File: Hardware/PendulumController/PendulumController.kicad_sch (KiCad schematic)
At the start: 12 parts, among them J101 MOTOR, J102 ENCODER

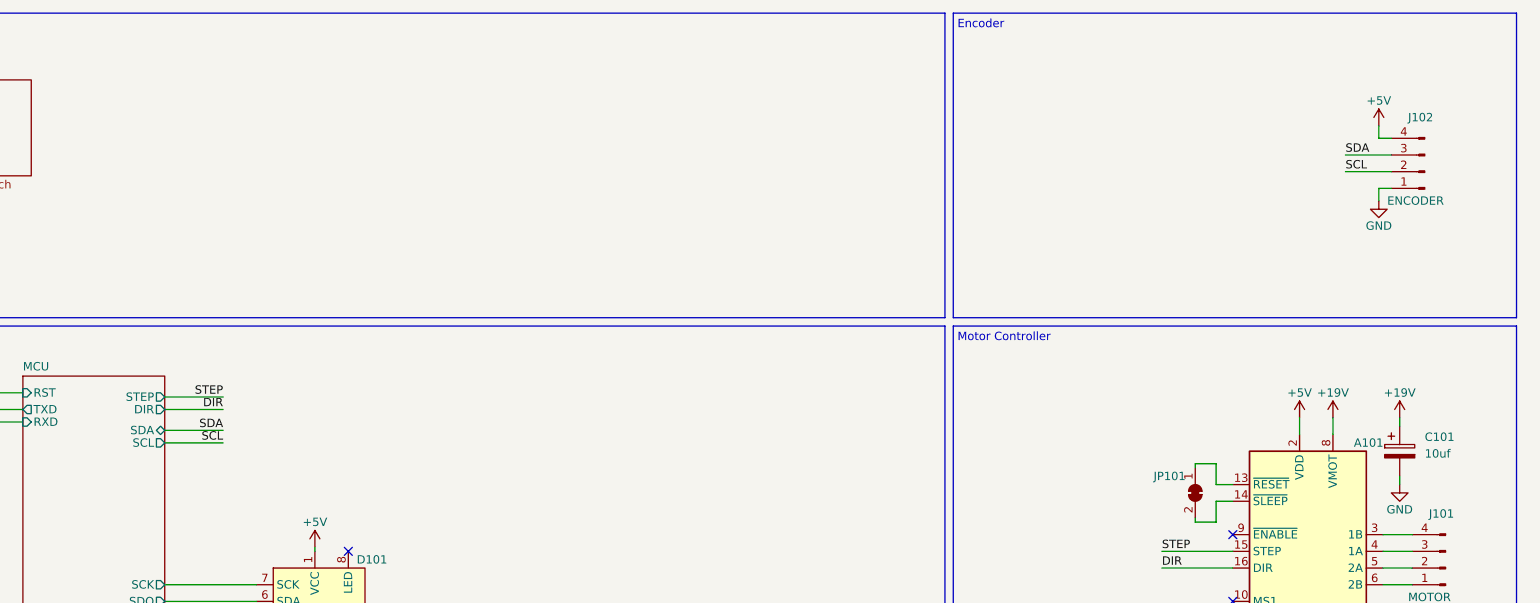
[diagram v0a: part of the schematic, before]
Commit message: Clean up board design with embedded power supply
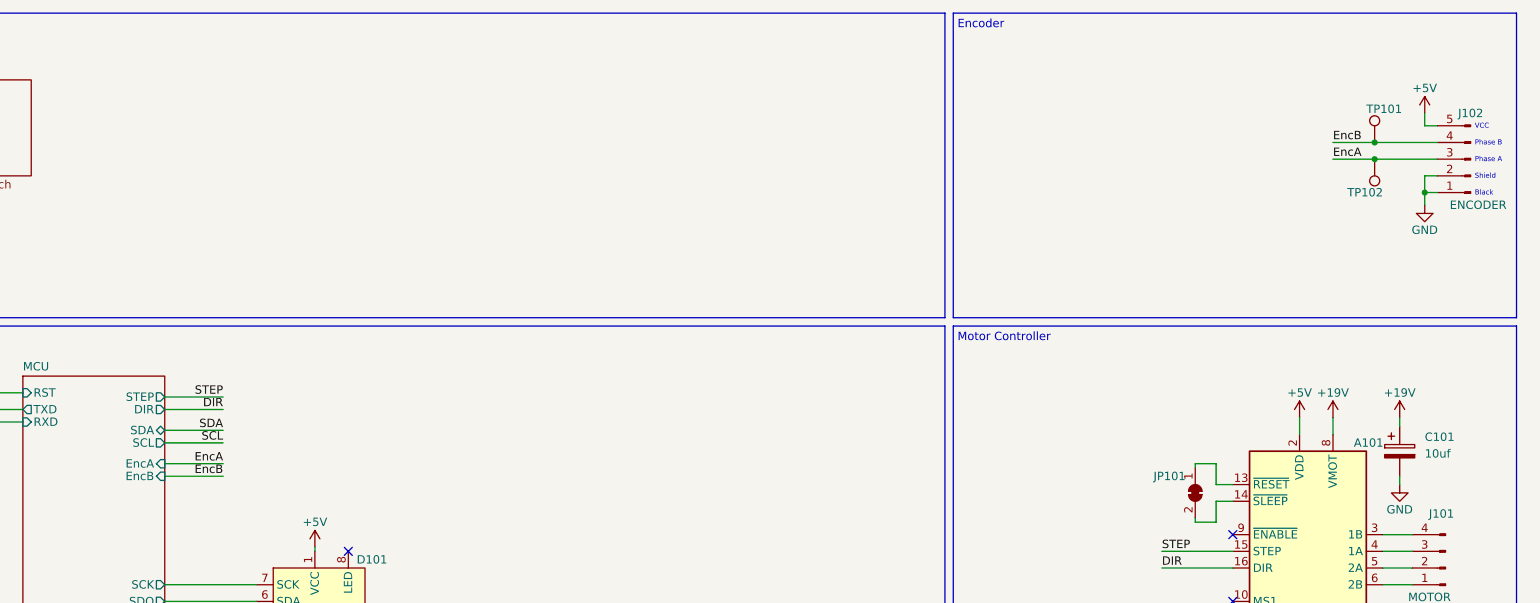
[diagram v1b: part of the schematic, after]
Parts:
- removed J102: ENCODER, Connector_JST:JST_EH_B4B-EH-A_1x04_P2.50mm_Vertical, symbol Connector:Conn_01x04_Male
- added J102: ENCODER, Connector_JST:JST_EH_B5B-EH-A_1x05_P2.50mm_Vertical, symbol Connector:Conn_01x05_Male
- added TP101, TP102: TestPoint, TestPoint:TestPoint_Pad_1.5x1.5mm, symbol Connector:TestPoint
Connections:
- net +5V: now also J102.5 (Pin_5)
- net GND: now also J102.1 (Pin_1), J102.2 (Pin_2)
- new net EncA: J102.3 (Pin_3), TP102.1
- new net EncB: J102.4 (Pin_4), TP101.1
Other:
- sheet MCU ports: added EncA, EncB; removed none
- note added: "Black"
- note added: "Phase A"
- note added: "Phase B"
- note added: "Shield"
- note added: "VCC"

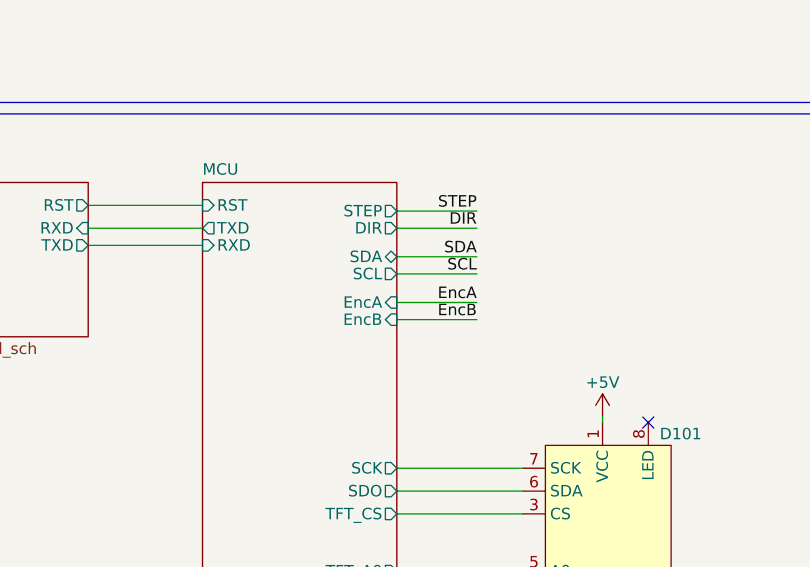
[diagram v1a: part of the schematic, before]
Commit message: Fix DRC check
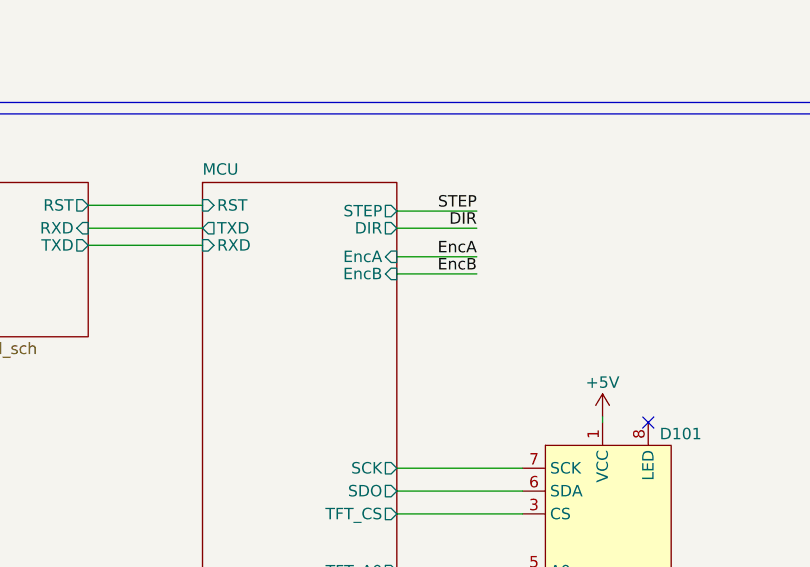
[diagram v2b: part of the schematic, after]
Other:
- sheet MCU ports: added none; removed SCL, SDA
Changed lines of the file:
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@@
     (stroke (width 0) (type default) (color 0 0 0 0))
   )
-  (wire (pts (xy 76.835 84.455) (xy 85.725 84.455))
+  (wire (pts (xy 76.835 79.375) (xy 85.725 79.375))
     (stroke (width 0) (type default) (color 0 0 0 0))
   )
@@
     (stroke (width 0) (type default) (color 0 0 0 0))
   )
-  (wire (pts (xy 76.835 79.375) (xy 85.725 79.375))
-    (stroke (width 0) (type default) (color 0 0 0 0))
-  )
-  (wire (pts (xy 76.835 82.55) (xy 85.725 82.55))
+  (wire (pts (xy 76.835 77.47) (xy 85.725 77.47))
     (stroke (width 0) (type default) (color 0 0 0 0))
   )
@@
   )
   (wire (pts (xy 233.68 83.185) (xy 233.68 82.55))
-    (stroke (width 0) (type default) (color 0 0 0 0))
-  )
-  (wire (pts (xy 76.835 77.47) (xy 85.725 77.47))
     (stroke (width 0) (type default) (color 0 0 0 0))
   )
@@
     (effects (font (size 1.27 1.27)) (justify left bottom))
   )
-  (label "SDA" (at 85.725 77.47 180)
-    (effects (font (size 1.27 1.27)) (justify right bottom))
-  )
   (label "STEP" (at 228.6 95.885 0)
     (effects (font (size 1.27 1.27)) (justify left bottom))
@@
     (effects (font (size 1.27 1.27)) (justify right bottom))
   )
-  (label "EncB" (at 85.725 84.455 180)
+  (label "EncB" (at 85.725 79.375 180)
     (effects (font (size 1.27 1.27)) (justify right bottom))
   )
-  (label "EncA" (at 85.725 82.55 180)
-    (effects (font (size 1.27 1.27)) (justify right bottom))
-  )
-  (label "SCL" (at 85.725 79.375 180)
+  (label "EncA" (at 85.725 77.47 180)
     (effects (font (size 1.27 1.27)) (justify right bottom))
   )
@@
       (effects (font (size 1.27 1.27)) (justify right))
     )
-    (pin "SDA" bidirectional (at 76.835 77.47 0)
-      (effects (font (size 1.27 1.27)) (justify right))
-    )
-    (pin "SCL" output (at 76.835 79.375 0)
-      (effects (font (size 1.27 1.27)) (justify right))
-    )
     (pin "SCK" output (at 76.835 100.965 0)
       (effects (font (size 1.27 1.27)) (justify right))
@@
       (effects (font (size 1.27 1.27)) (justify right))
     )
-    (pin "EncB" input (at 76.835 84.455 0)
-      (effects (font (size 1.27 1.27)) (justify right))
-    )
-    (pin "EncA" input (at 76.835 82.55 0)
-      (effects (font (size 1.27 1.27)) (justify right))
-    )
+    (pin "EncB" input (at 76.835 79.375 0)
+      (effects (font (size 1.27 1.27)) (justify right))
+    )
+    (pin "EncA" input (at 76.835 77.47 0)
+      (effects (font (size 1.27 1.27)) (justify right))
+    )

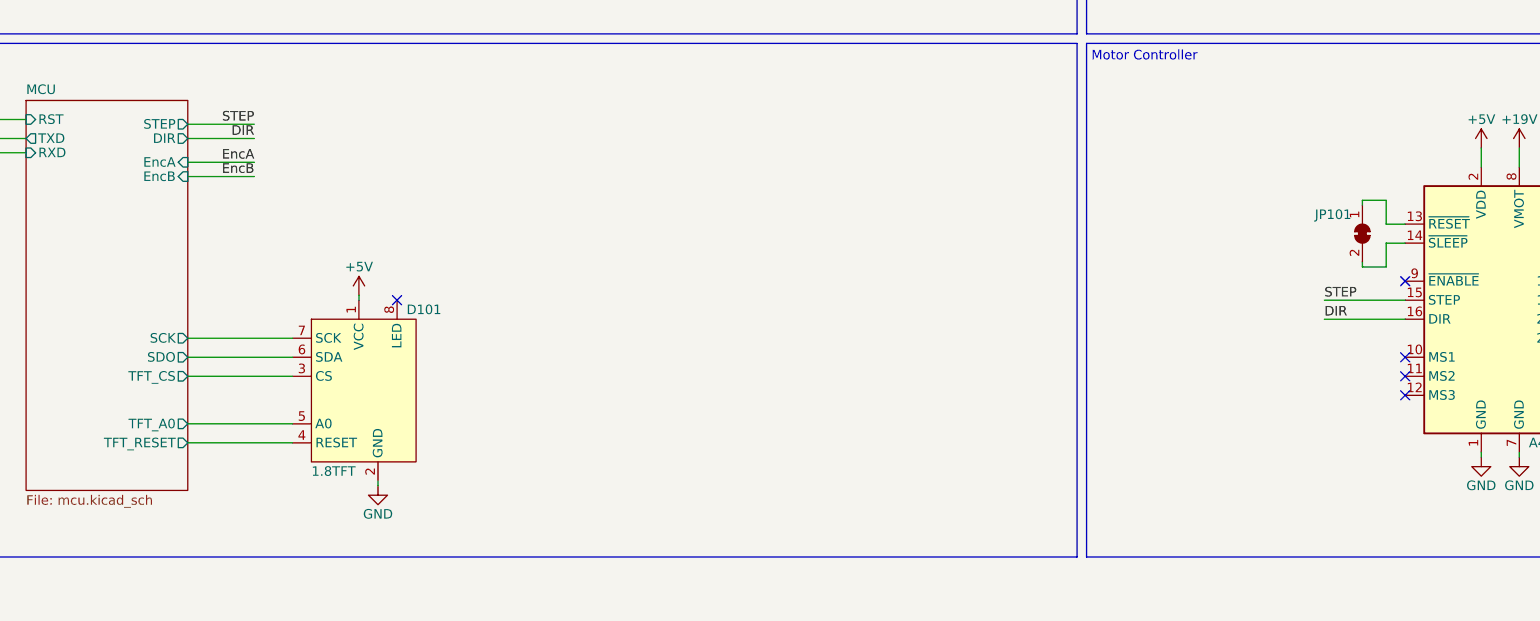
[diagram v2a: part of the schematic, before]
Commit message: Check backlight power circuit before printing
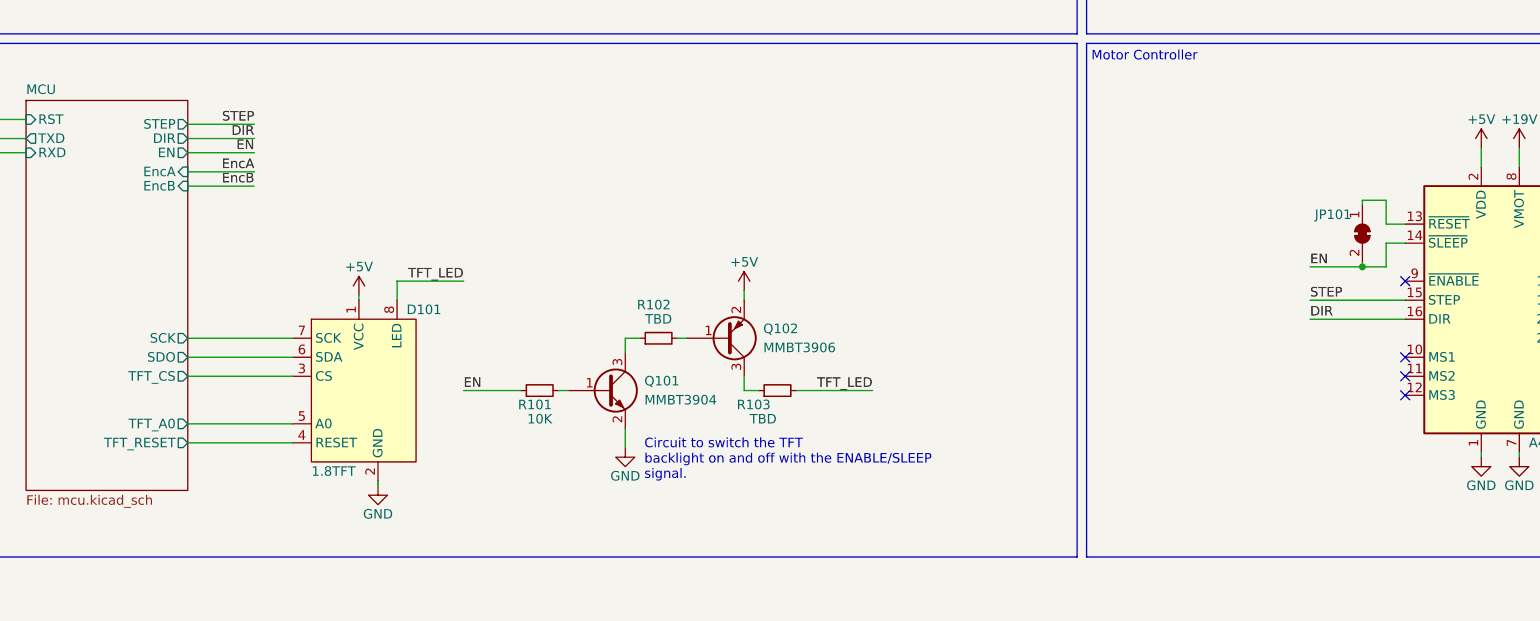
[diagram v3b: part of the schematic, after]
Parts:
- added Q101: MMBT3904, Package_TO_SOT_SMD:SOT-23, symbol Transistor_BJT:MMBT3904
- added Q102: MMBT3906, Package_TO_SOT_SMD:SOT-23, symbol Transistor_BJT:MMBT3906
- added R101: 10K, Resistor_SMD:R_0805_2012Metric, symbol Device:R_Small
- added R102, R103: TBD, Resistor_SMD:R_0805_2012Metric, symbol Device:R_Small
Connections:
- net +5V: now also Q102.2 (E)
- net GND: now also Q101.2 (E)
- net TFT_LED: now reaches D101.8 (LED)
- net TFT_LED: now also R103.2
- net EN: now reaches A101.14 (~{SLEEP}), JP101.2 (B)
- net EN: now also R101.1
- new net: Q101.1 (B), R101.2
- new net: Q101.3 (C), R102.1
- new net: Q102.3 (C), R103.1
- new net: Q102.1 (B), R102.2
- no-connect marks 5 -> 4
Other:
- sheet MCU ports: added EN; removed none
- note added: "Circuit to switch the TFT backlight on and off with the ENABLE/SLEEP signal."
